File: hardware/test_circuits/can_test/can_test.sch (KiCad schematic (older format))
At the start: 37 parts, among them J1 Conn_01x05_Female, SW1 SW_Push, SW2 SW_Push, SW3 SW_SPDT, U1 PIC18F4620-IP, U2 L7805, Y1 10MHz

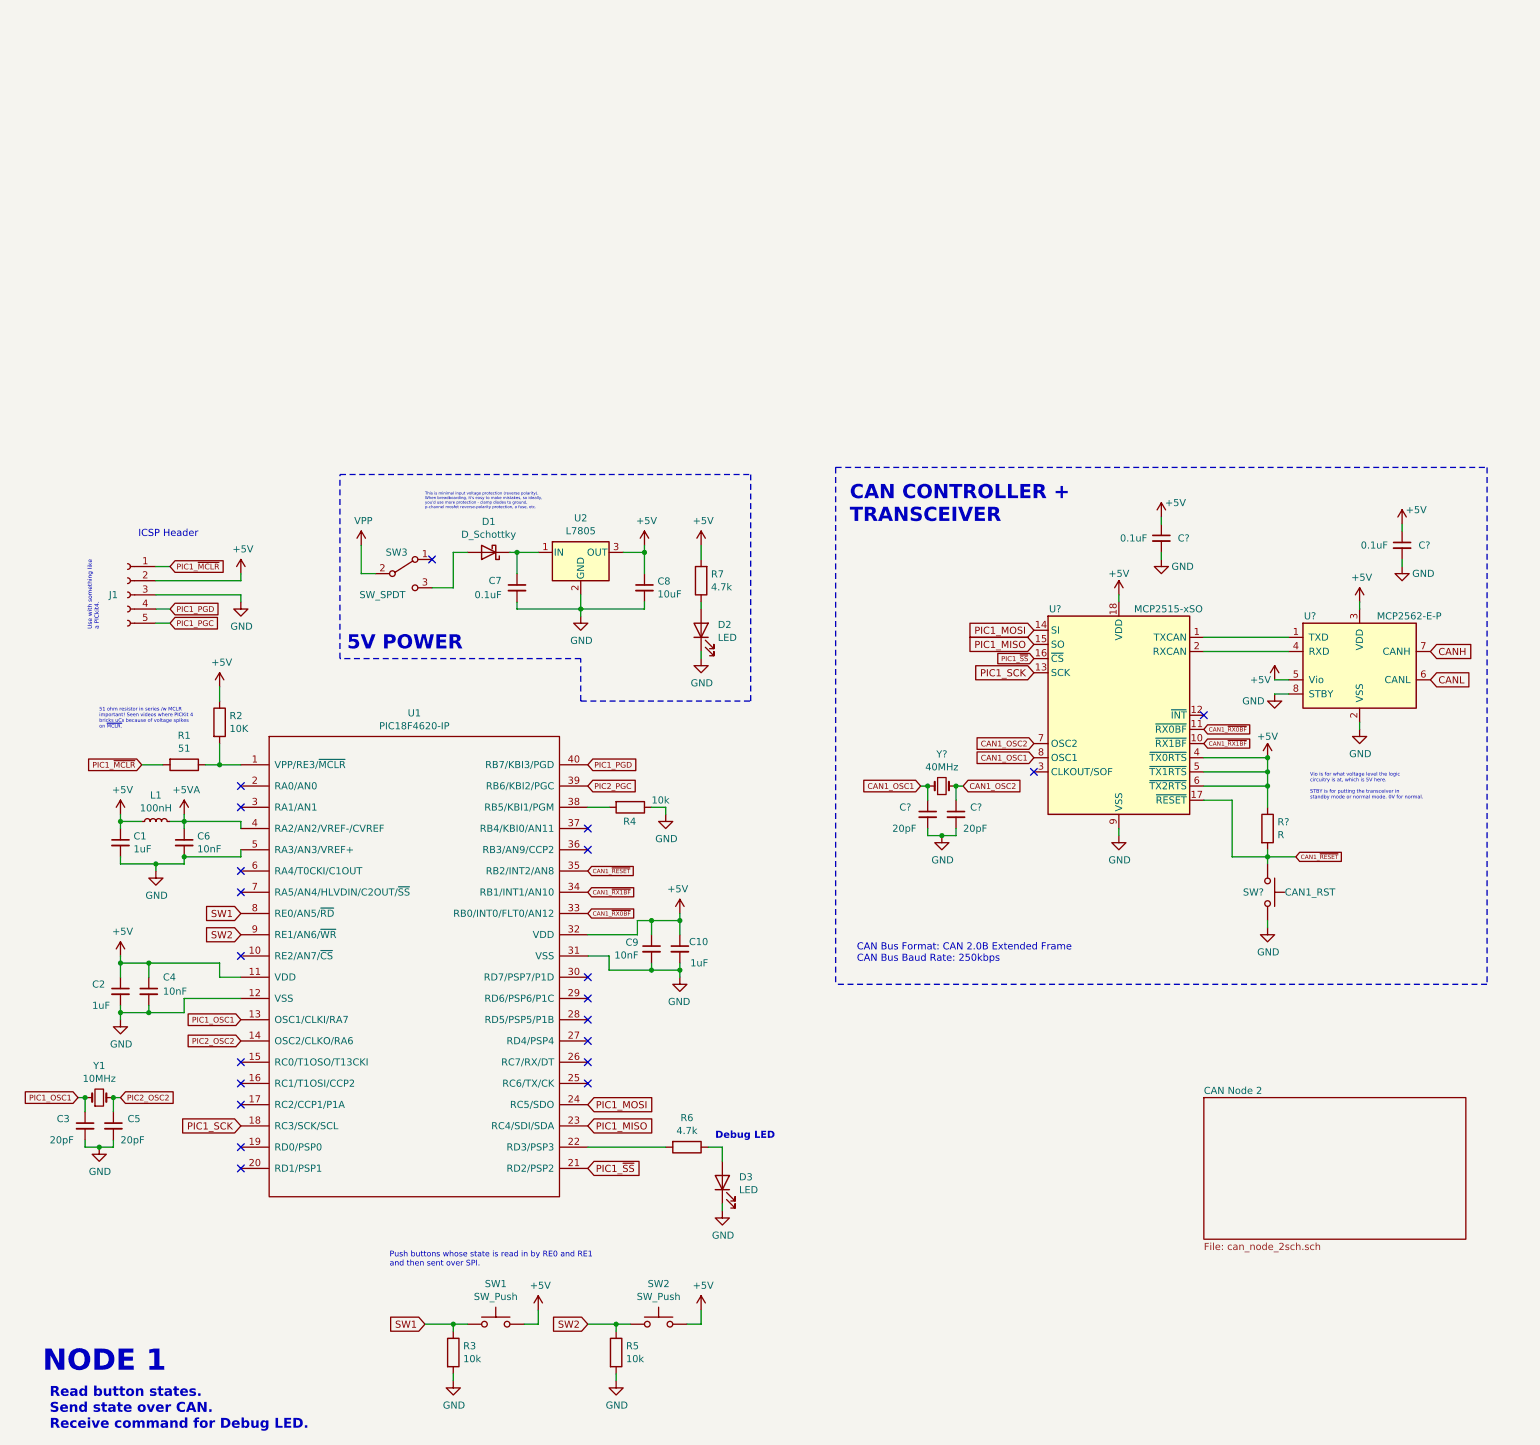
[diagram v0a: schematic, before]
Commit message: Finished CAN Test schematic now. Also added schematics for the individual elements used so that it would make it easier to reuse for later schematics!
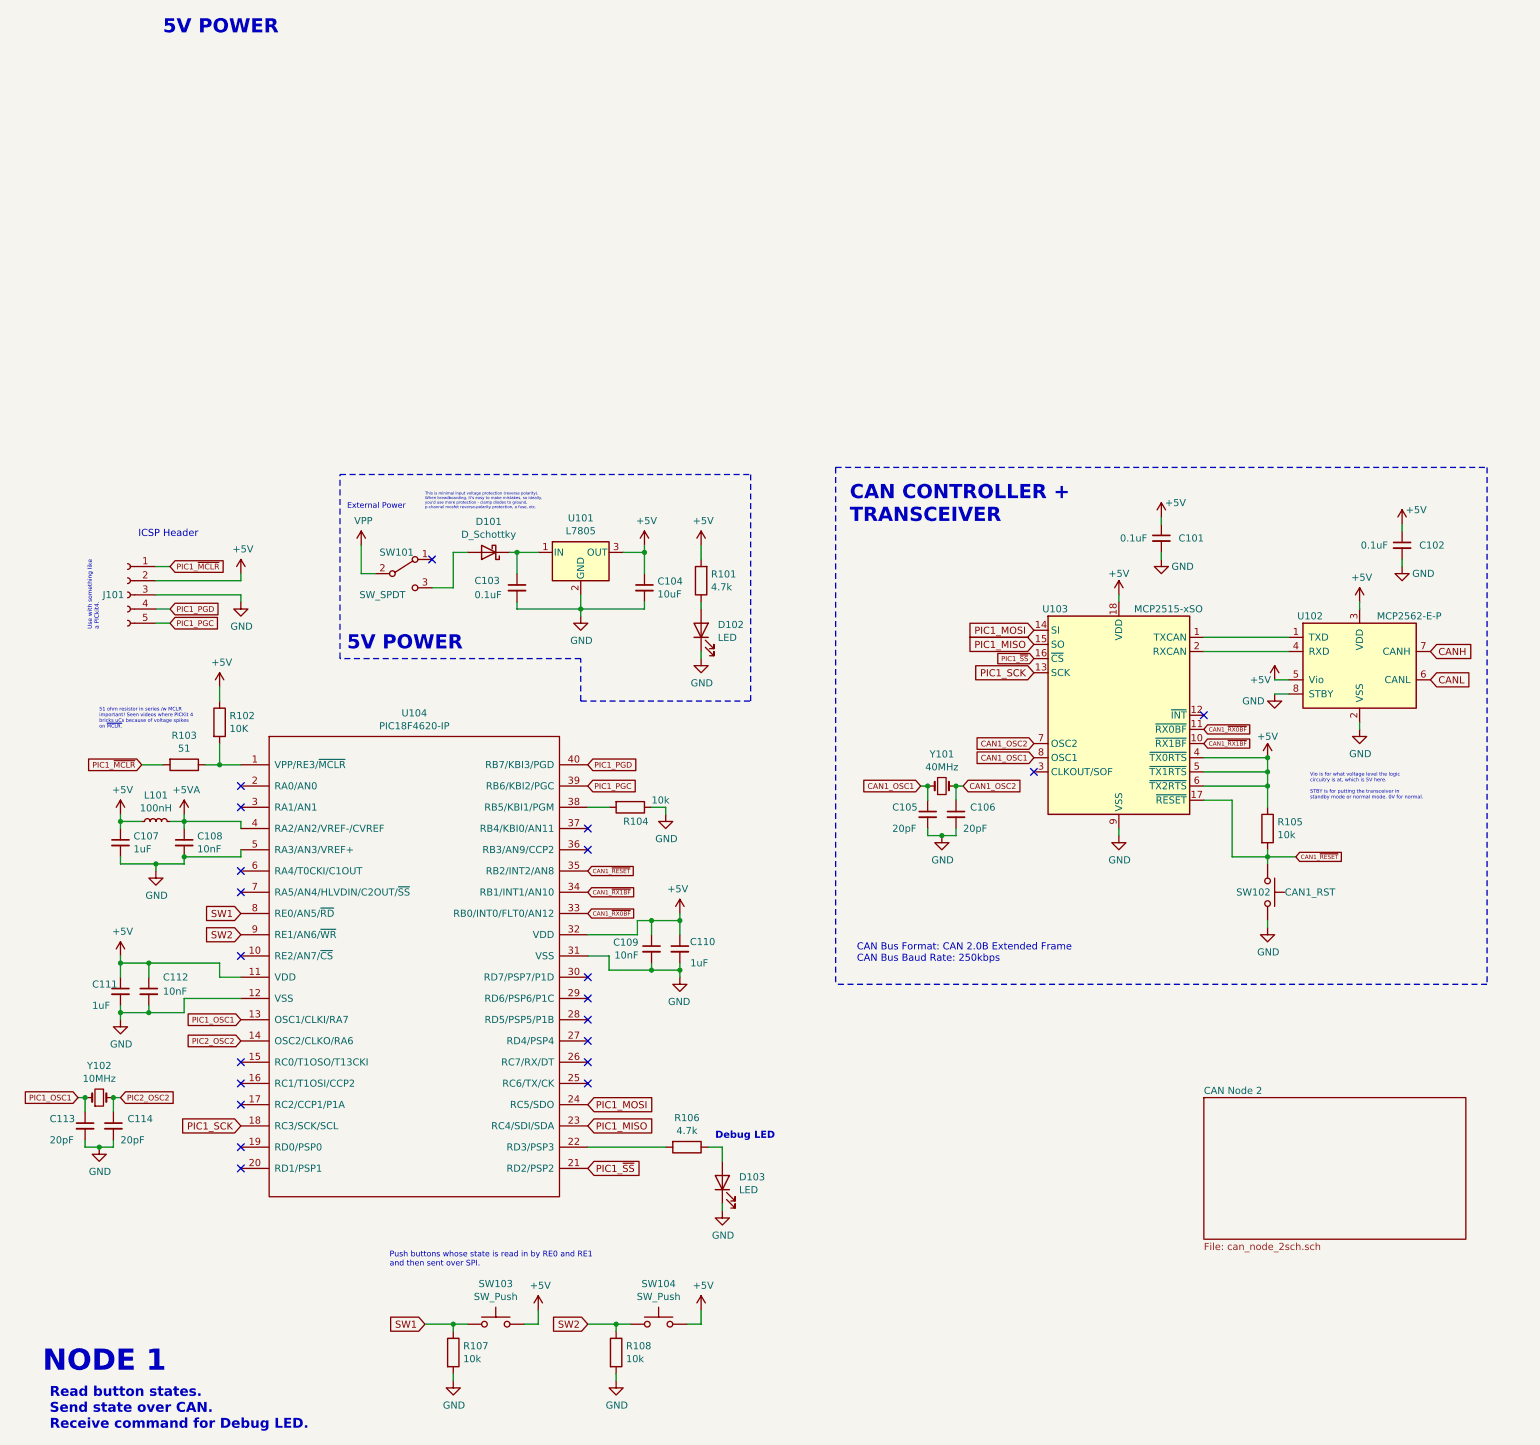
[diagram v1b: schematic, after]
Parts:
- R105: renamed from R?; value R -> 10k
- gave numbers to parts that had none: 8
- renumbered C7 to C103, C8 to C104, C1 to C107, C6 to C108, C9 to C109, C10 to C110, C2 to C111, C4 to C112, C3 to C113, C5 to C114, D1 to D101, D2 to D102, D3 to D103, J1 to J101, L1 to L101, R7 to R101, R2 to R102, R1 to R103, R4 to R104, R6 to R106, R3 to R107, R5 to R108, SW3 to SW101, SW1 to SW103, SW2 to SW104, U2 to U101, U1 to U104, Y1 to Y102
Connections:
- net PIC2_PGC is gone; now on net PIC1_PGC: U104.39 (RB6/KBI2/PGC)
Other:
- note added: "External Power"

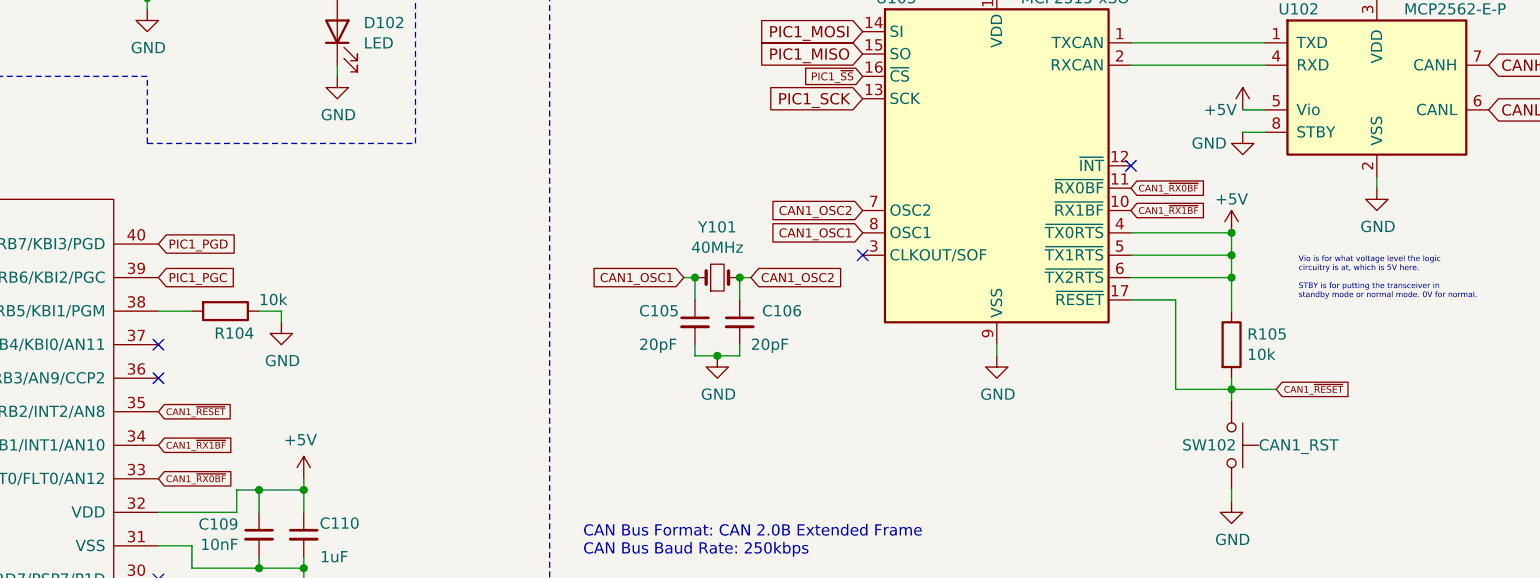
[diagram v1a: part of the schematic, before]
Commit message: Realized I probably want to actually use the ~INT pin on the MCP2515 for recognizing when a transmission has successfull occured... And if I'm using that, might as well also use it for RX interrupts as well...
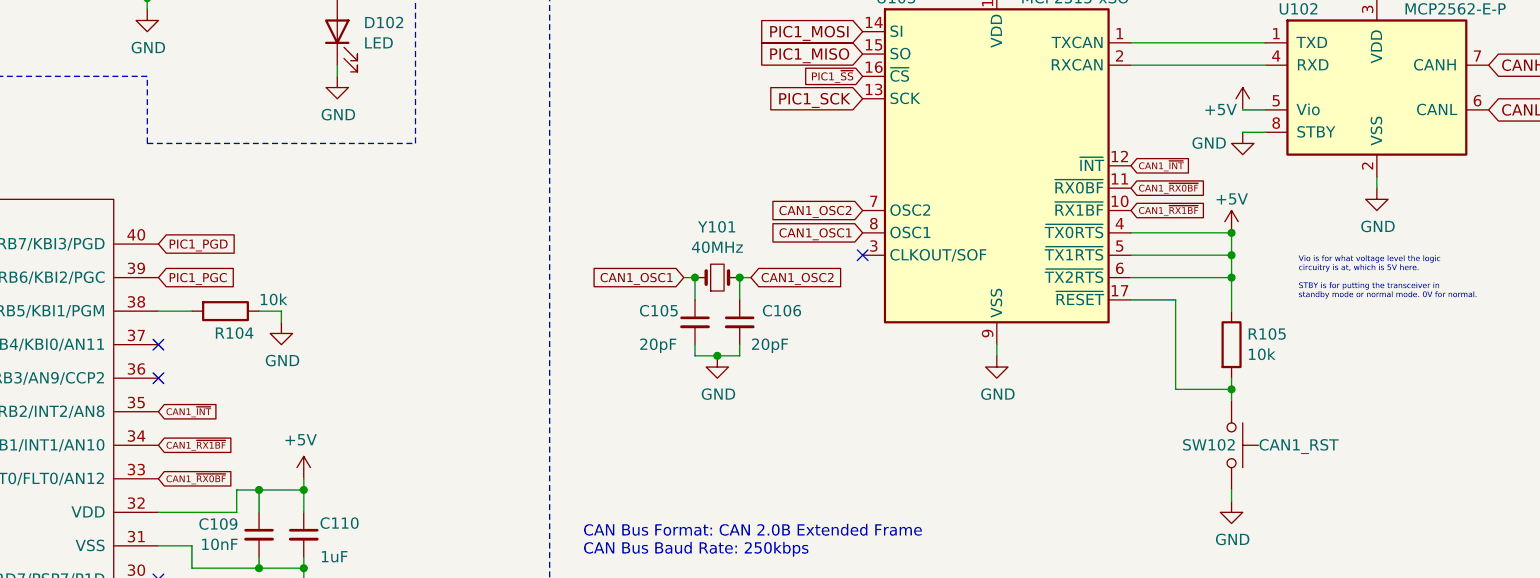
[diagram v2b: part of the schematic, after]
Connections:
- net CAN1_~INT: now reaches U103.12 (~INT)
- net CAN1_~INT: now also U104.35 (RB2/INT2/AN8)
- net CAN1_~RESET: no longer names the net of R105.2, SW102.1, U103.17 (~RESET)
- net CAN1_~RESET: no longer U104.35 (RB2/INT2/AN8)
- no-connect marks 21 -> 20
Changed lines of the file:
@@
 	5150 3050 5150 3100
 Text GLabel 4600 3500 2    30   Input ~ 0
-CAN1_~RESET
+CAN1_~INT
 $Comp
 L Interface_CAN_LIN:MCP2562-E-P U102
@@
 	1    0    0    -1
 $EndComp
-NoConn ~ 8950 2400
 Text GLabel 7750 1800 0    50   Input ~ 0
 PIC1_MOSI
@@
 Wire Wire Line
 	9400 3900 9400 3850
-Text GLabel 9600 3400 2    30   Input ~ 0
-CAN1_~RESET
-Wire Wire Line
-	9400 3400 9600 3400
+Text GLabel 8950 2400 2    30   Input ~ 0
+CAN1_~INT
 $Comp
 L power:+5V #PWR0101

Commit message: ..
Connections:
- net +5V: now also U103.10 (~RX1BF), U103.11 (~RX0BF)
- net CAN1_~INT: now also U104.33 (RB0/INT0/FLT0/AN12); no longer U104.35 (RB2/INT2/AN8)
- removed net CAN1_~RX0BF: U103.11 (~RX0BF), U104.33 (RB0/INT0/FLT0/AN12)
- net CAN1_~RX1BF: no longer names the net of U104.34 (RB1/INT1/AN10)
- net CAN1_~RX1BF: no longer U103.10 (~RX1BF)
- no-connect marks 20 -> 22
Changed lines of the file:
@@
 	1    0    0    -1
 $EndComp
-Text GLabel 4600 3800 2    30   Input ~ 0
-CAN1_~RX0BF
-Text GLabel 4600 3650 2    30   Input ~ 0
-CAN1_~RX1BF
 Wire Wire Line
 	5250 3800 5250 3850
@@
 Wire Wire Line
 	5150 3050 5150 3100
-Text GLabel 4600 3500 2    30   Input ~ 0
+Text GLabel 4600 3800 2    30   Input ~ 0
 CAN1_~INT
 $Comp
@@
 Wire Wire Line
 	8950 1950 9550 1950
-Text GLabel 8950 2500 2    30   Input ~ 0
-CAN1_~RX0BF
-Text GLabel 8950 2600 2    30   Input ~ 0
-CAN1_~RX1BF
 $Comp
 L Switch:SW_Push SW102
@@
 L power:+5V #PWR0118
 U 1 1 619123F1
-P 9400 2700
-F 0 "#PWR0118" H 9400 2550 50  0001 C CNN
-F 1 "+5V" H 9400 2850 50  0000 C CNN
-F 2 "" H 9400 2700 50  0001 C CNN
-F 3 "" H 9400 2700 50  0001 C CNN
-	1    9400 2700
+P 9400 2500
+F 0 "#PWR0118" H 9400 2350 50  0001 C CNN
+F 1 "+5V" H 9500 2550 50  0000 C CNN
+F 2 "" H 9400 2500 50  0001 C CNN
+F 3 "" H 9400 2500 50  0001 C CNN
+	1    9400 2500
 	1    0    0    -1
 $EndComp
@@
 Wire Wire Line
 	9400 2800 9400 2700
-Connection ~ 9400 2700
 Wire Wire Line
 	8950 2900 9400 2900
@@
 Text Notes 2900 950  0    40   ~ 0
 External Power
+Wire Wire Line
+	8950 2500 9400 2500
+Wire Wire Line
+	9400 2700 9400 2600
+Connection ~ 9400 2700
+Connection ~ 9400 2500
+Wire Wire Line
+	8950 2600 9400 2600
+Connection ~ 9400 2600
+Wire Wire Line
+	9400 2600 9400 2500
+NoConn ~ 4600 3650
+NoConn ~ 4600 3500
 $EndSCHEMATC

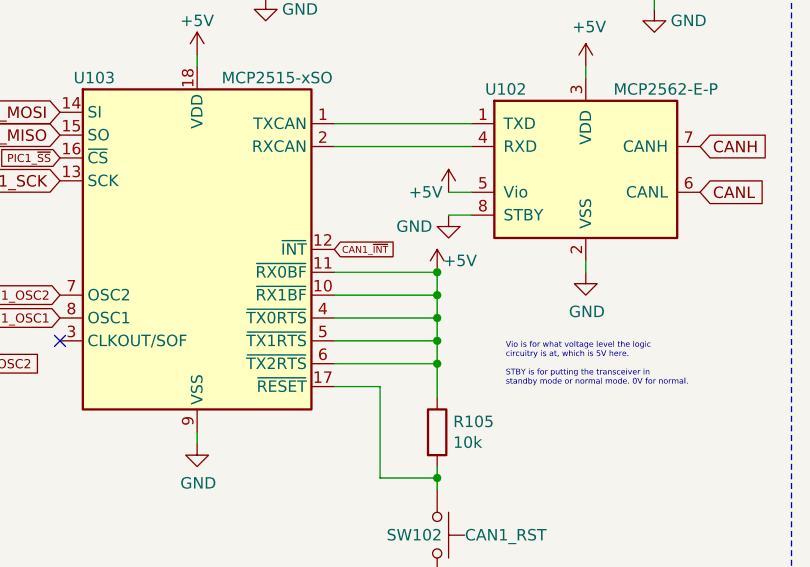
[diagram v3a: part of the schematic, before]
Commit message: Complete the can_send routine --> will need to set up ISR as well still! Will include this as a comment at the end of the mcp2515.c file.
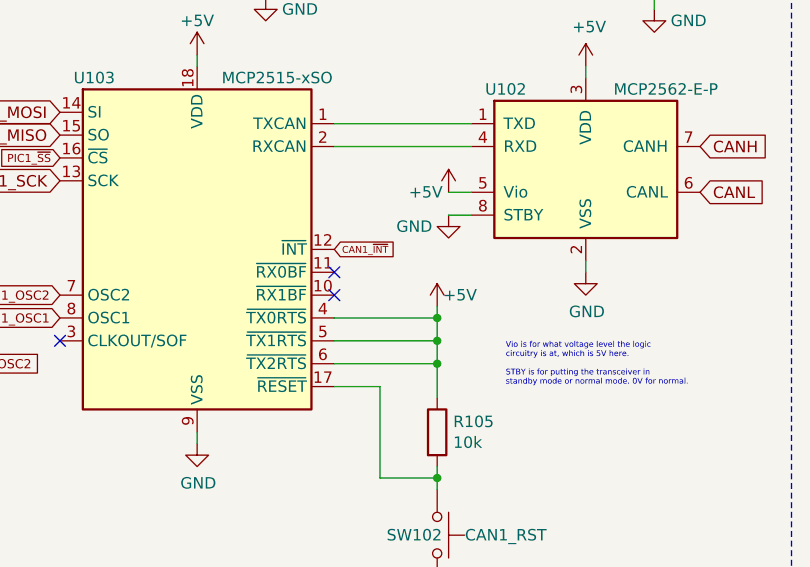
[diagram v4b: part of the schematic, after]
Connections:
- net +5V: no longer U103.10 (~RX1BF), U103.11 (~RX0BF)
- no-connect marks 22 -> 24
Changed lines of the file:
@@
 L power:+5V #PWR0118
 U 1 1 619123F1
-P 9400 2500
-F 0 "#PWR0118" H 9400 2350 50  0001 C CNN
-F 1 "+5V" H 9500 2550 50  0000 C CNN
-F 2 "" H 9400 2500 50  0001 C CNN
-F 3 "" H 9400 2500 50  0001 C CNN
-	1    9400 2500
+P 9400 2650
+F 0 "#PWR0118" H 9400 2500 50  0001 C CNN
+F 1 "+5V" H 9500 2700 50  0000 C CNN
+F 2 "" H 9400 2650 50  0001 C CNN
+F 3 "" H 9400 2650 50  0001 C CNN
+	1    9400 2650
 	1    0    0    -1
 $EndComp
@@
 Text Notes 2900 950  0    40   ~ 0
 External Power
-Wire Wire Line
-	8950 2500 9400 2500
-Wire Wire Line
-	9400 2700 9400 2600
 Connection ~ 9400 2700
-Connection ~ 9400 2500
-Wire Wire Line
-	8950 2600 9400 2600
-Connection ~ 9400 2600
-Wire Wire Line
-	9400 2600 9400 2500
 NoConn ~ 4600 3650
 NoConn ~ 4600 3500
+Wire Wire Line
+	9400 2650 9400 2700
+NoConn ~ 8950 2600
+NoConn ~ 8950 2500
 $EndSCHEMATC
